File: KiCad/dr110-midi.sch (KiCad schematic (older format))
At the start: 22 parts, among them J1 Conn_01x12_Male, J2 Conn_01x02_Male, Q1 BC547, Q2 BC547, Q3 BC547, Q4 BC547, Q5 BC547, Q6 BC547, Q7 BC547, U1 6N138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

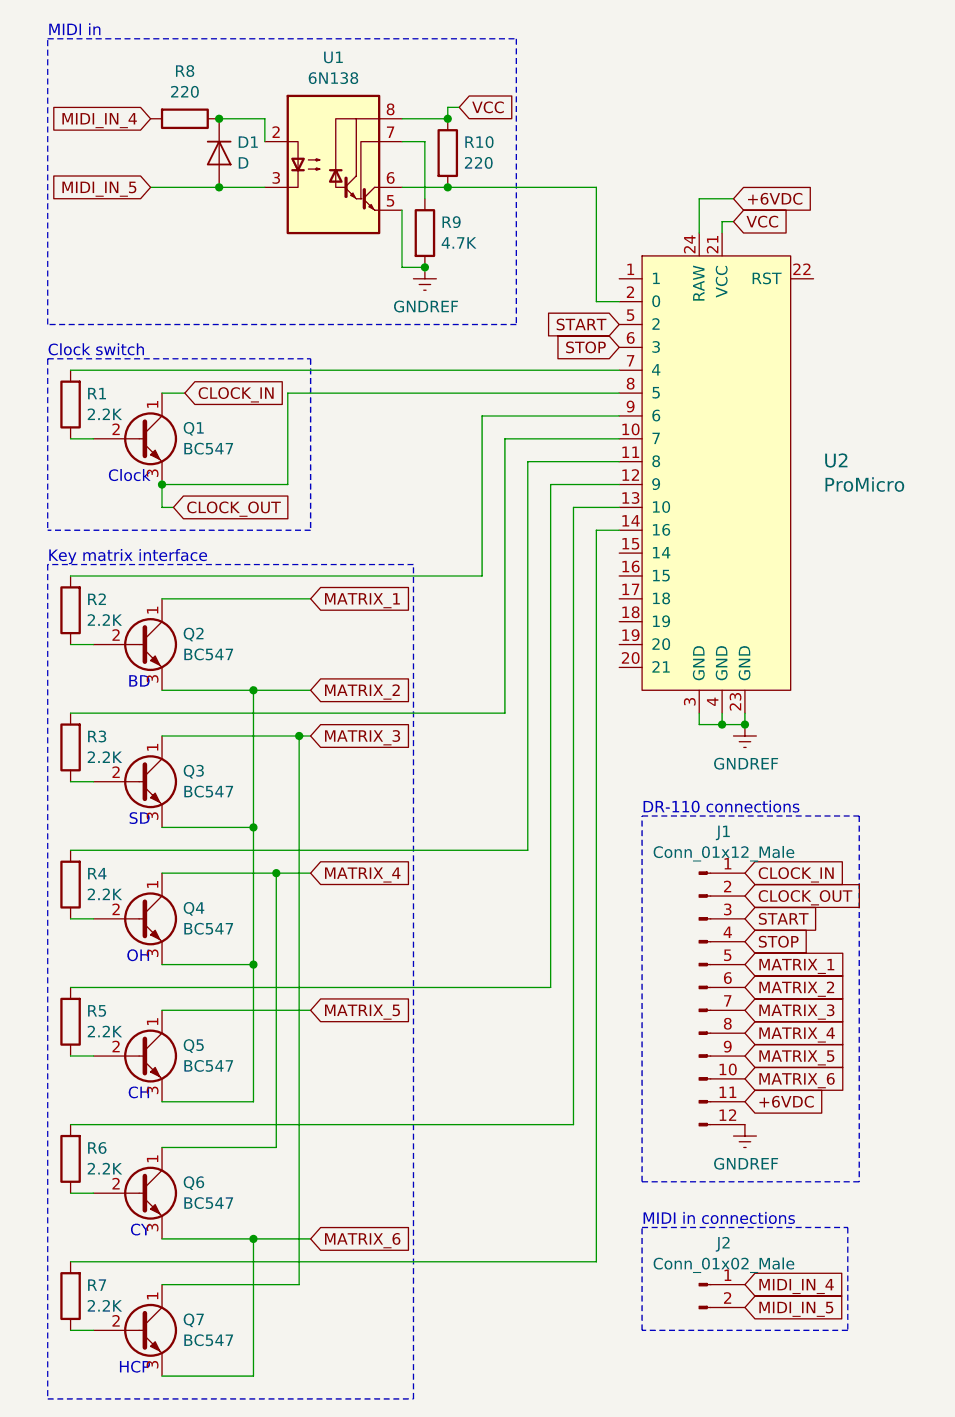
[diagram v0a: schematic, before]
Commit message: Fix key matrix transistor pinouts.
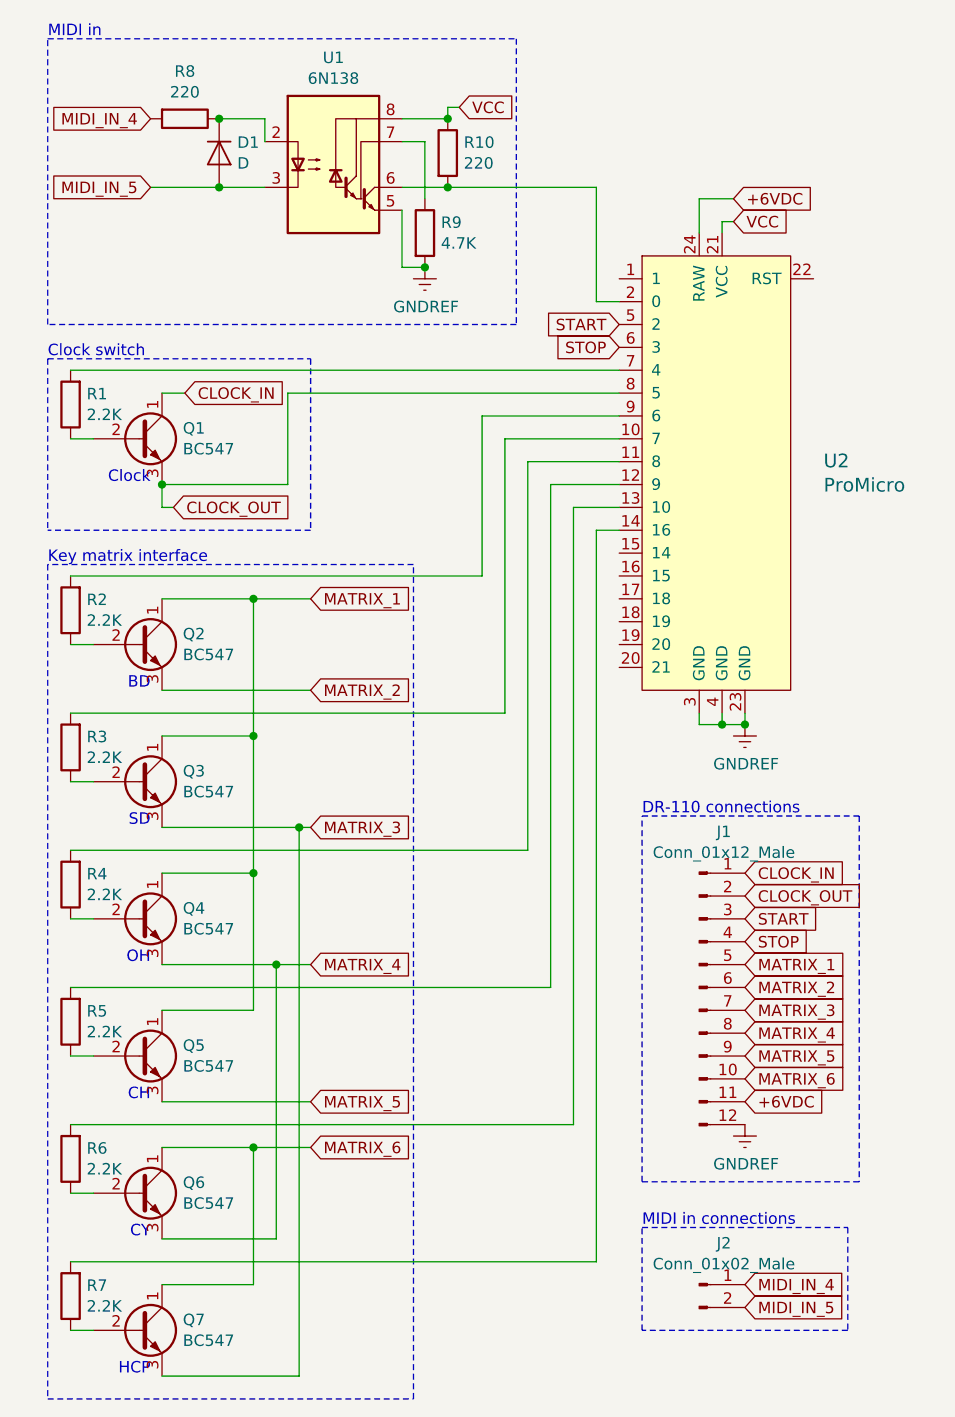
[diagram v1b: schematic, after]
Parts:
- D1: footprint Diodes_THT:D_DO-35_SOD27_P7.62mm_Horizontal -> Diodes_THT:D_DO-35_SOD27_P5.08mm_Vertical_KathodeUp
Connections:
- net MATRIX_1: now also Q3.1 (C), Q4.1 (C), Q5.1 (C)
- net MATRIX_2: no longer Q3.3 (E), Q4.3 (E), Q5.3 (E)
- net MATRIX_3: now also Q3.3 (E), Q7.3 (E); no longer Q3.1 (C), Q7.1 (C)
- net MATRIX_4: now also Q4.3 (E), Q6.3 (E); no longer Q4.1 (C), Q6.1 (C)
- net MATRIX_5: now also Q5.3 (E); no longer Q5.1 (C)
- net MATRIX_6: now also Q6.1 (C), Q7.1 (C); no longer Q6.3 (E), Q7.3 (E)
